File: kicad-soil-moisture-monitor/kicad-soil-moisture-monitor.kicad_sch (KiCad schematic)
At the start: 2 parts, among them U2 AM2302, U3 ESP32-C3-DevKitM-1

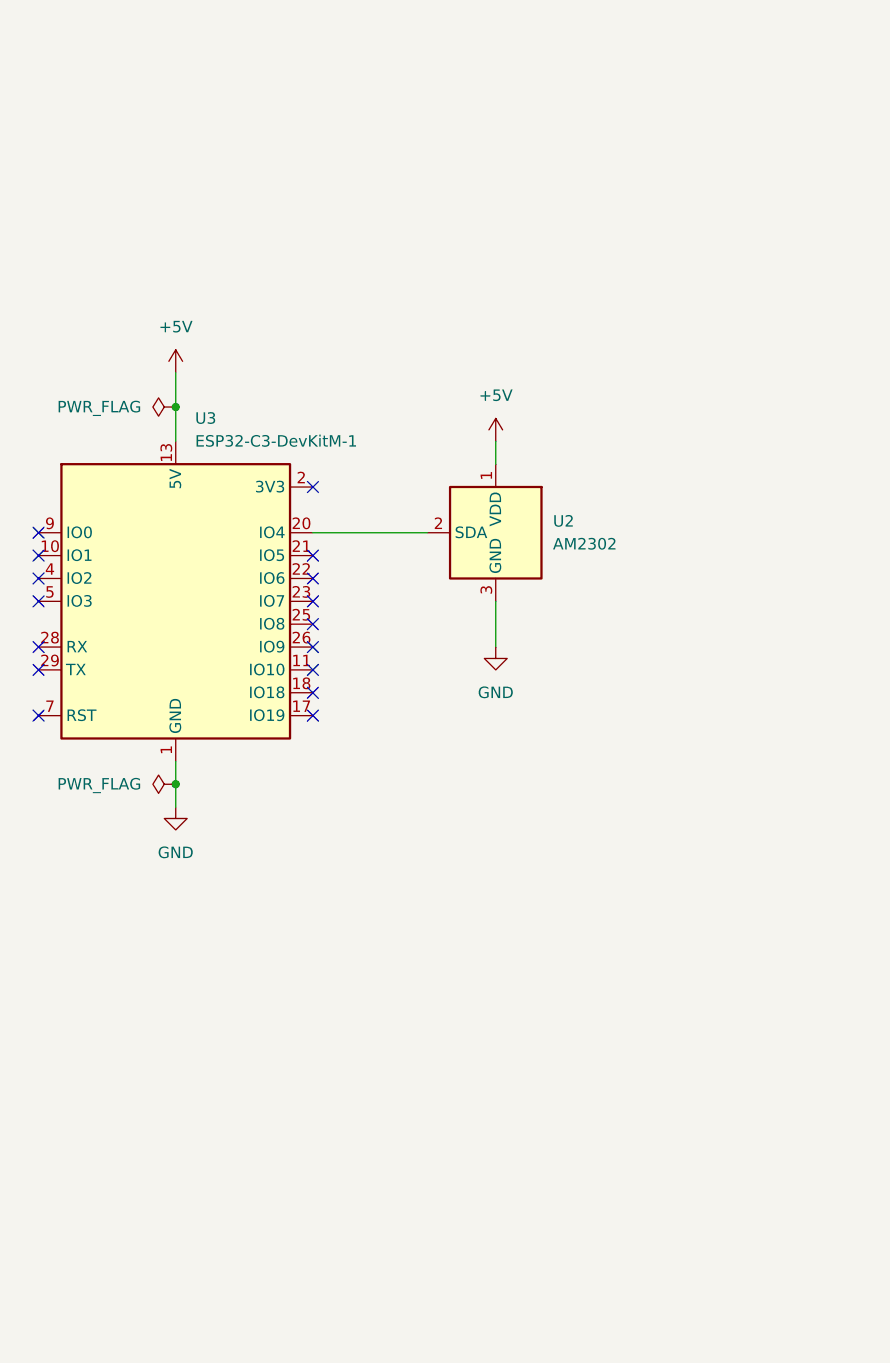
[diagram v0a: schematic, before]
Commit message: feat: Fix battery reading, update readme and add schematic.
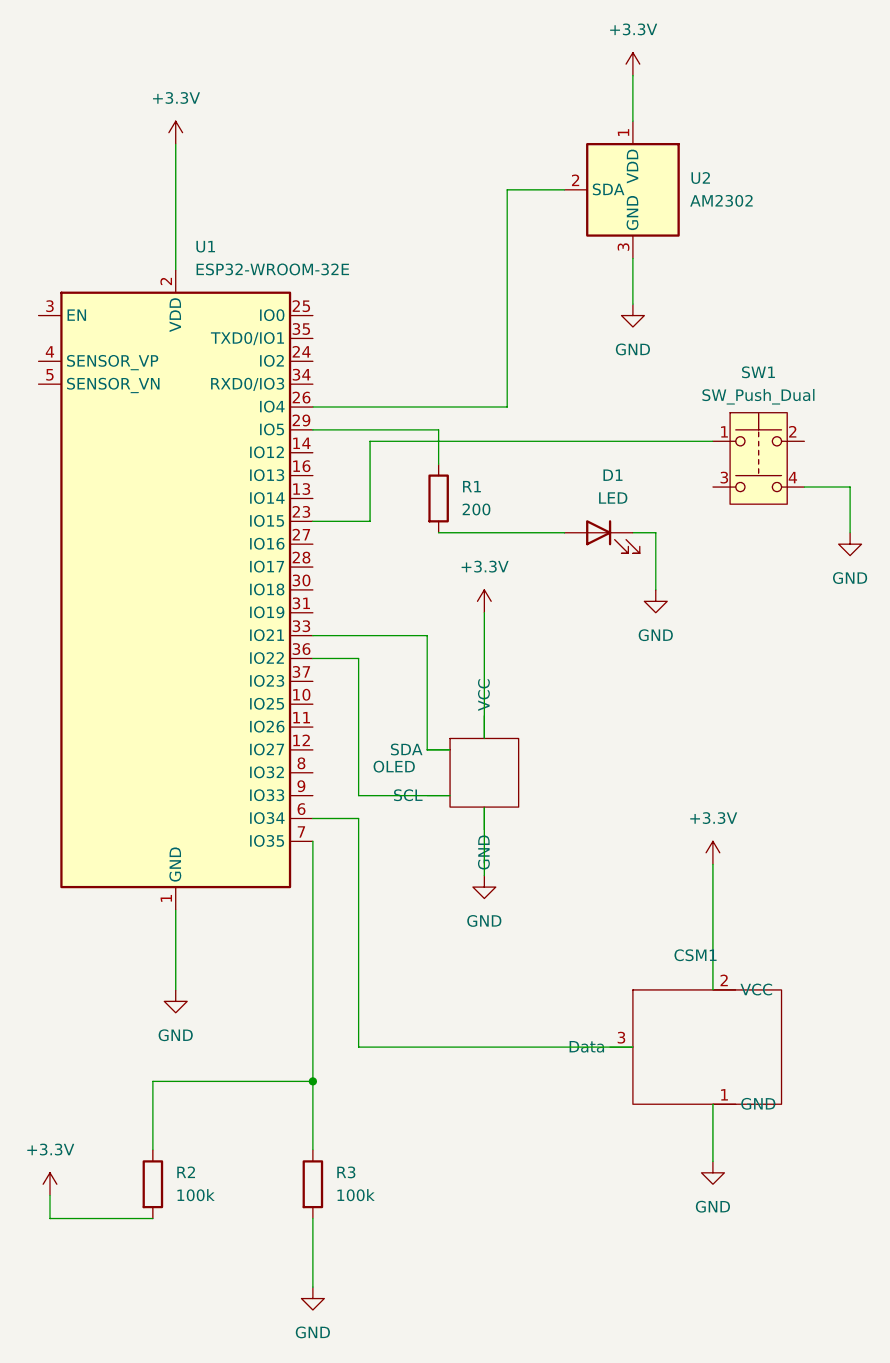
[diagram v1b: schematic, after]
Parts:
- removed U3: ESP32-C3-DevKitM-1, RF_Module:ESP32-C3-DevKitM-1, symbol RF_Module:ESP32-C3-DevKitM-1
- added CSM1: ~, symbol symbol_lib:Capacitive Soil Moisture
- added D1: LED, symbol Device:LED
- added OLED: ~, symbol symbol_lib:OLED
- added R1: 200, symbol Device:R
- added R2, R3: 100k, symbol Device:R
- added SW1: SW_Push_Dual, symbol Switch:SW_Push_Dual
- added U1: ESP32-WROOM-32E, RF_Module:ESP32-WROOM-32D, symbol RF_Module:ESP32-WROOM-32E
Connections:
- net GND: now also CSM1.1 (GND), D1.1 (K), OLED. (GND), R3.2, SW1.4, U1.1 (GND), U1.15 (GND), U1.38 (GND), U1.39 (GND)
- net at U2.2 (SDA): now also U1.26 (IO4)
- net +5V renamed +3.3V
- net +3.3V: now also CSM1.2 (VCC), OLED. (GND), R2.2, U1.2 (VDD)
- new net: R1.1, U1.29 (IO5)
- new net: D1.2 (A), R1.2
- new net: OLED. (GND), U1.33 (IO21)
- new net: OLED. (GND), U1.36 (IO22)
- new net: SW1.1, U1.23 (IO15)
- new net: CSM1.3 (Data), U1.6 (IO34)
- new net: R2.1, R3.1, U1.7 (IO35)
- no-connect marks 16 -> 0
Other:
- moved on the sheet: U2
